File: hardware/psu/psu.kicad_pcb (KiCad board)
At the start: 4 copper layers, 42 x 100 mm, 46 parts, among them J1 Conn_02x08_Odd_Even, J2 Conn_02x02_Odd_Even, J3 USB_C_Receptacle_USB2.0_14P, J4 USB_A, Q1 DMP3056LSS, SW1 SW_SPDT, U1 REC30K-2412DZ, U2 CH224A, U3 AP63301WU

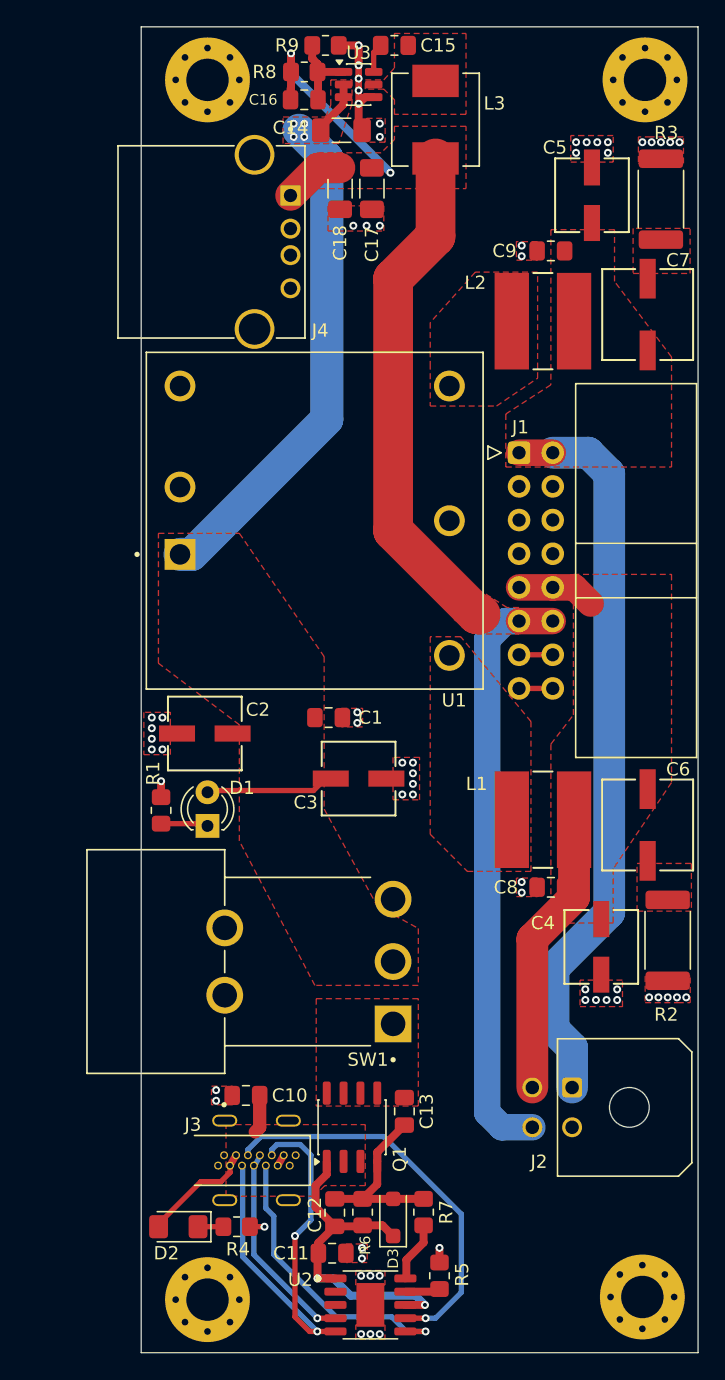
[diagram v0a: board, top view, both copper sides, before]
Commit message: Version 1.1 board. Measurements complete, updated power on switch design, refined in-rush limiting
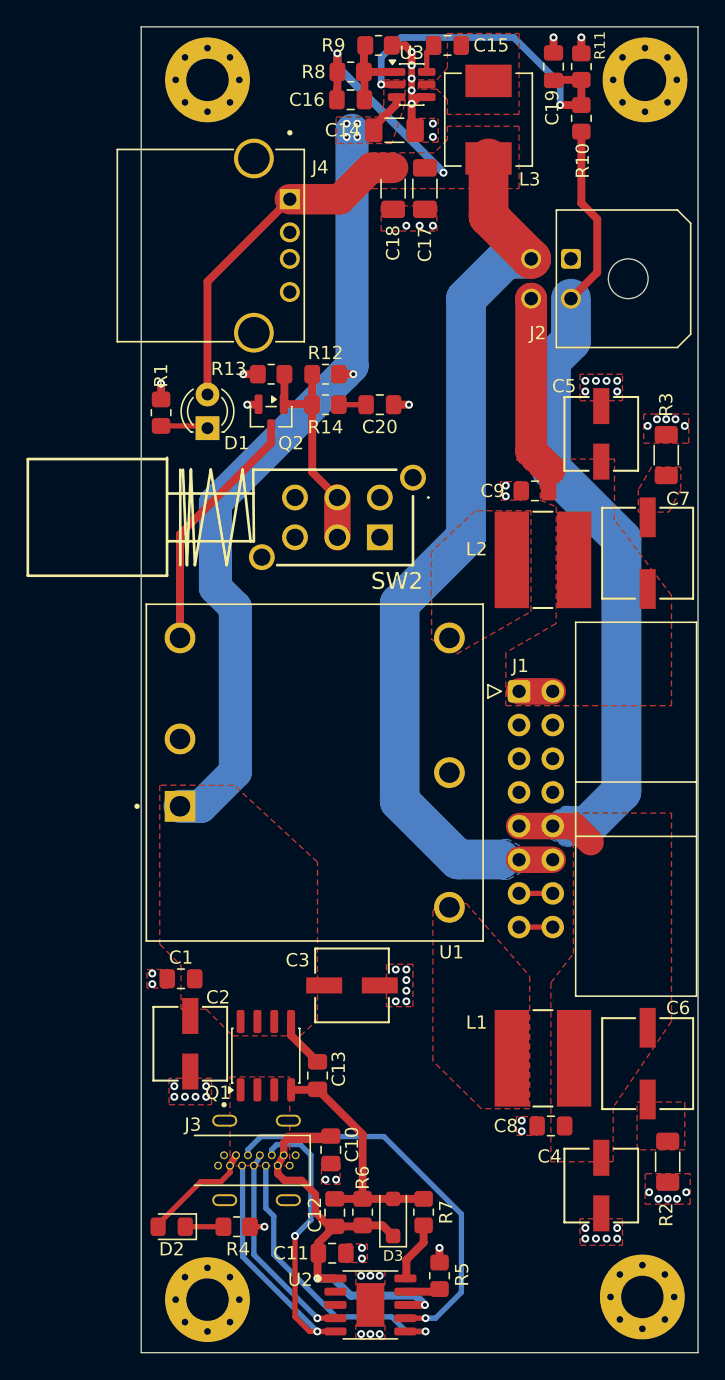
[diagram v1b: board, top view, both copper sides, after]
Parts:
- removed SW1: SW_SPDT, Switches:SW_300SP1J1BLKM6QE
- added C19: 100n, Capacitor_SMD:C_0805_2012Metric_Pad1.18x1.45mm_HandSolder, F.Cu at (131.1, 53.0)
- added C20: 1u, Capacitor_SMD:C_0805_2012Metric_Pad1.18x1.45mm_HandSolder, F.Cu at (118.0, 78.5)
- added Q2: 2N7002, Package_TO_SOT_SMD:SOT-23, F.Cu at (109.8, 79.4)
- added R10: 100k, Resistor_SMD:R_0805_2012Metric_Pad1.20x1.40mm_HandSolder, F.Cu at (133.2, 56.9)
- added R11: 47k, Resistor_SMD:R_0805_2012Metric_Pad1.20x1.40mm_HandSolder, F.Cu at (133.2, 53.0)
- added R12: 15k, Resistor_SMD:R_0805_2012Metric_Pad1.20x1.40mm_HandSolder, F.Cu at (113.9, 76.2)
- added R13: 15k, Resistor_SMD:R_0805_2012Metric_Pad1.20x1.40mm_HandSolder, F.Cu at (109.8, 76.2)
- added R14: 220, Resistor_SMD:R_0805_2012Metric_Pad1.20x1.40mm_HandSolder, F.Cu at (113.9, 78.5)
- added SW2: SW_Slide_DPDT, Switches:SW_DPDT_LC2255EENP, F.Cu at (118.0, 87.0)
- C12: value 100n -> 1u
- D2: footprint LED_SMD:LED_1206_3216Metric_Pad1.42x1.75mm_HandSolder -> LED_SMD:LED_0805_2012Metric_Pad1.15x1.40mm_HandSolder
- R1: value 4k7 -> 2k2
- R2, R3: footprint Resistor_SMD:R_2512_6332Metric_Pad1.40x3.35mm_HandSolder -> Resistor_SMD:R_1206_3216Metric_Pad1.30x1.75mm_HandSolder
- R7: value 1k0 -> 4k7
- moved J2 62.5 mm to (132.4, 67.5)
- moved D1 30.0 mm to (105.0, 80.3)
- moved R1 30.0 mm to (101.5, 79.1)
- moved C2 23.4 mm to (103.7, 126.7), turned to -90 degrees
- moved C1 22.6 mm to (103.0, 121.8), turned to 0 degrees
- moved R3 19.3 mm to (139.6, 82.3)
- moved U1 19.0 mm to (113.1, 106.2)
- moved C9 18.1 mm to (129.7, 85.0)
- moved C5 18.0 mm to (134.7, 80.7)
- moved C4 18.0 mm to (134.7, 137.4)
- moved C7 18.0 mm to (138.2, 89.7)
- moved C8 18.0 mm to (130.9, 132.9)
- moved J1 18.0 mm to (128.5, 100.1)
- moved L1 18.0 mm to (130.3, 127.8)
- moved L2 18.0 mm to (130.3, 90.2)
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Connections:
- C13 pad 1: VUSB_C -> VDC_SYS
- D1 pad 2: VDC_SYS -> +5V
- J2 pad 1: -12V -> GND
- J2 pad 2: GND -> +12V
- J2 pad 3: +12V -> +5V
- J2 pad 4: +5V -> -12V
- Q1 pad 5: VUSB_C -> VDC_SYS
- Q1 pad 6: VUSB_C -> VDC_SYS
- Q1 pad 7: VUSB_C -> VDC_SYS
- Q1 pad 8: VUSB_C -> VDC_SYS
- U1 pad 3: unconnected-(U1-CTRL-Pad3) -> Net-(Q2-D)
- U3 pad 2: VDC_SYS -> Net-(U3-EN)
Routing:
- net -12V: track 56.1 -> 16.0 mm
- net +12V: track 27.4 -> 64.8 mm
- net Net-(U3-EN): track 0.00 -> 26.0 mm, vias 0 -> 2
- net Net-(Q2-D): track 0.00 -> 18.6 mm
- net DC_PWR_ON: track 0.00 -> 17.5 mm
- net VDC_SYS: track 52.0 -> 66.9 mm, vias 4 -> 5
- net GND: track 12.8 -> 18.0 mm, vias 63 -> 68
- net +5V: track 104.7 -> 109.9 mm
- net Net-(D3-A): track 13.7 -> 18.5 mm
- net VBUS_IN: track 39.3 -> 42.7 mm
- net Net-(C20-Pad2): track 0.00 -> 2.06 mm
- net Net-(D2-K): track 2.02 -> 2.77 mm
- added copper zone on B.Cu, net +12V
- added copper zone on B.Cu, net +5V
- removed copper zone on F.Cu, net VUSB_C
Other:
- board text added: "idyllm CC BY-SA 4.0 v1.1.20260626"
- board text removed: "idyllm CC BY-SA 4.0 v1.0.20260524"
